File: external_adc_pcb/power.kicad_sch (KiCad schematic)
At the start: 12 parts, among them U25 TPS7A2033PDBVR, U26 TLV9061xDBV

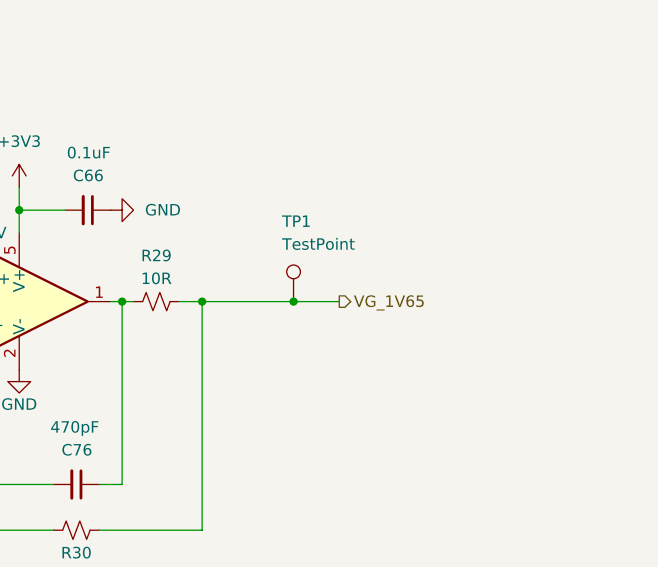
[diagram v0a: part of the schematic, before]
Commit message: adjust VG issue for internal ADC version; changed naming for VG
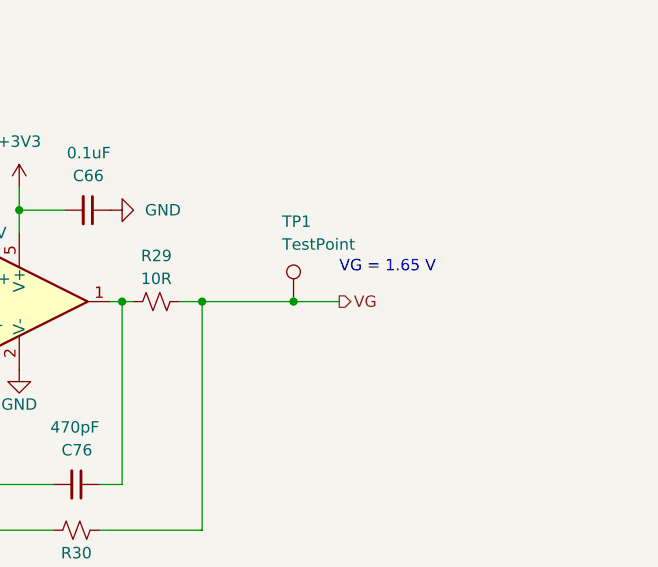
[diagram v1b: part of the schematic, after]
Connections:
- net VG_1V65 renamed VG
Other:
- note added: "VG = 1.65 V"
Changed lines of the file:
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@@
+		)
+	)
+	(text "VG = 1.65 V"
+		(exclude_from_sim no)
+		(at 177.8 73.66 0)
+		(effects
+			(font
+				(face "Iosevka NF")
+				(size 1.27 1.27)
+			)
+			(justify left)
 		)
 	)
@@
 		)
 	)
-	(hierarchical_label "VG_1V65"
+	(hierarchical_label "VG"
 		(shape output)
 		(at 177.8 77.47 0)
